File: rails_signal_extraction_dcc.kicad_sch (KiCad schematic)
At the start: 1 part

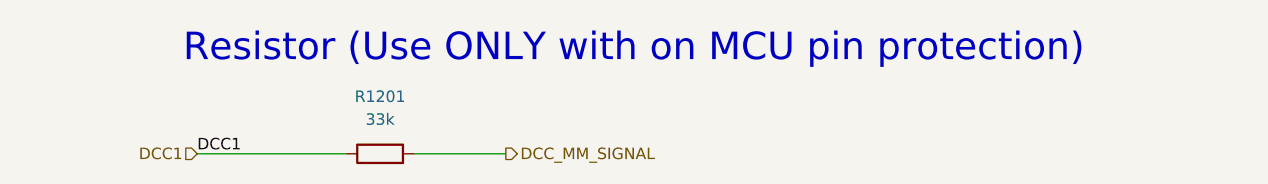
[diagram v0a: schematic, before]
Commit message: Fix - rail_signal_extract (ERC)
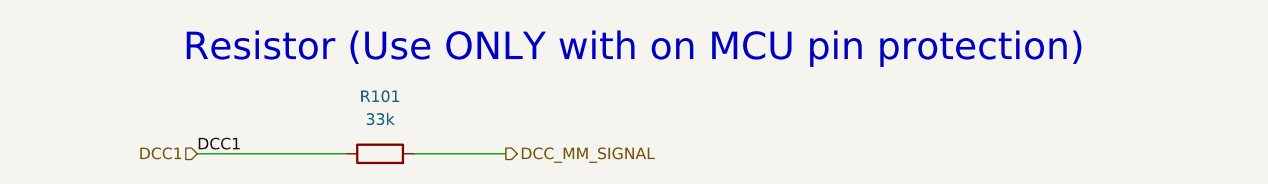
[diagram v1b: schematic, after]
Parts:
- renumbered R1201 to R101
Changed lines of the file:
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@@
 		(dnp no)
 		(fields_autoplaced yes)
-		(property "Reference" "R1201"
+		(property "Reference" "R101"
 			(at 52.07 31.75 90)
 			(effects
@@
 		)
 		(instances
+			(project "rails_signal_extraction_dcc_test"
+				(path "/f9a870df-aaf2-427d-b524-30792058699c/2112ffae-5e6c-42bd-91fd-dac3de454b63"
+					(reference "R101")
+					(unit 1)
+				)
+			)
 			(project "xDuinoRails-Fortuna-M"
 				(path "/fb33ec4e-6596-45d2-a121-8d3475acd69a/c9229de7-1ed3-435d-9b11-33fa2e05ec65/3f6df3ac-cacb-4a62-a6cd-afb105728627"
